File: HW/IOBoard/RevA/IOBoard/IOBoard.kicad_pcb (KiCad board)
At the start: 2 copper layers, 35.6 x 61 mm, 8 parts, among them J1 Conn_02x05_Odd_Even, J2 Conn_Coaxial, J3 Conn_Coaxial, J4 Conn_Coaxial

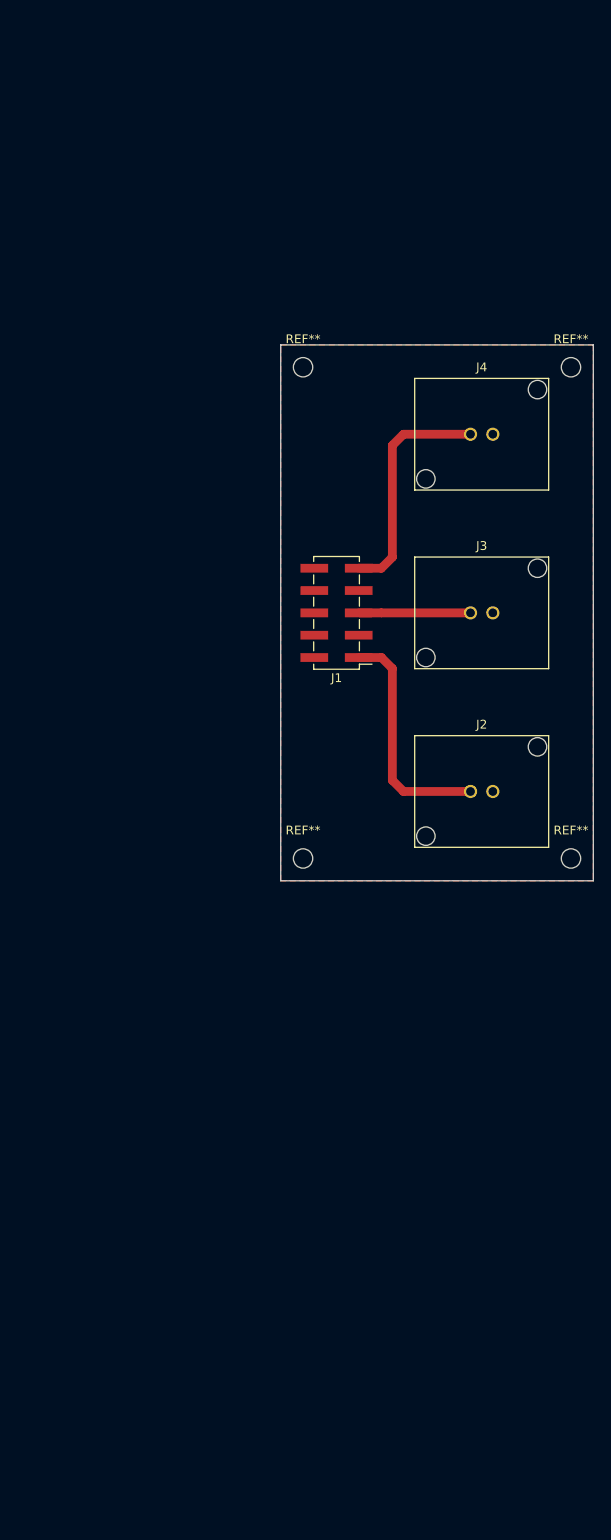
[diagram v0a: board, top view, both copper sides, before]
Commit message: updated front panel board layouts
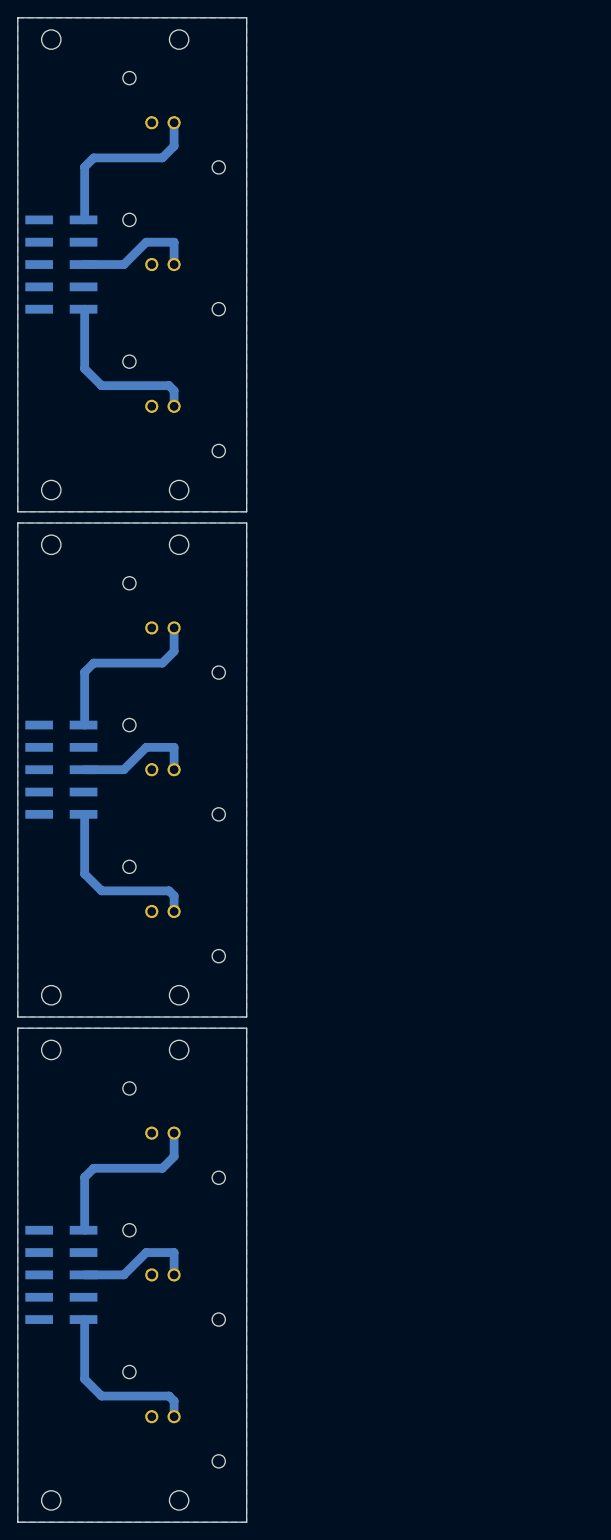
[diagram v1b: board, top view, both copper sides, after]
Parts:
- removed the J1 at (161.3, 85.1)
- removed the J2 at (177.8, 105.4)
- removed the J3 at (177.8, 85.1)
- removed the J4 at (177.8, 64.8)
- removed the REF** at (188.0, 113.0)
- removed the REF** at (157.5, 113.0)
- removed the REF** at (157.5, 57.1)
- removed the REF** at (188.0, 57.1)
- added J1: Conn_02x05_Odd_Even, Connector_PinHeader_2.54mm:PinHeader_2x05_P2.54mm_Vertical_SMD, B.Cu at (130.0, 160.4)
- added J1: Conn_02x05_Odd_Even, Connector_PinHeader_2.54mm:PinHeader_2x05_P2.54mm_Vertical_SMD, B.Cu at (130.0, 102.9)
- added J1: Conn_02x05_Odd_Even, Connector_PinHeader_2.54mm:PinHeader_2x05_P2.54mm_Vertical_SMD, B.Cu at (130.0, 45.5)
- added J2: Conn_Coaxial, RSProStraight50OhmPCBMountBulkheadFittingBNC_5260279:RSProStraight50OhmPCBMountBulkheadFittingBNC_5260279, B.Cu at (142.8, 144.3)
- added J2: Conn_Coaxial, RSProStraight50OhmPCBMountBulkheadFittingBNC_5260279:RSProStraight50OhmPCBMountBulkheadFittingBNC_5260279, B.Cu at (142.8, 86.8)
- added J2: Conn_Coaxial, RSProStraight50OhmPCBMountBulkheadFittingBNC_5260279:RSProStraight50OhmPCBMountBulkheadFittingBNC_5260279, B.Cu at (142.8, 29.3)
- added J3: Conn_Coaxial, RSProStraight50OhmPCBMountBulkheadFittingBNC_5260279:RSProStraight50OhmPCBMountBulkheadFittingBNC_5260279, B.Cu at (142.8, 160.4)
- added J3: Conn_Coaxial, RSProStraight50OhmPCBMountBulkheadFittingBNC_5260279:RSProStraight50OhmPCBMountBulkheadFittingBNC_5260279, B.Cu at (142.8, 102.9)
- added J3: Conn_Coaxial, RSProStraight50OhmPCBMountBulkheadFittingBNC_5260279:RSProStraight50OhmPCBMountBulkheadFittingBNC_5260279, B.Cu at (142.8, 45.5)
- added J4: Conn_Coaxial, RSProStraight50OhmPCBMountBulkheadFittingBNC_5260279:RSProStraight50OhmPCBMountBulkheadFittingBNC_5260279, B.Cu at (142.8, 176.5)
- added J4: Conn_Coaxial, RSProStraight50OhmPCBMountBulkheadFittingBNC_5260279:RSProStraight50OhmPCBMountBulkheadFittingBNC_5260279, B.Cu at (142.8, 119.1)
- added J4: Conn_Coaxial, RSProStraight50OhmPCBMountBulkheadFittingBNC_5260279:RSProStraight50OhmPCBMountBulkheadFittingBNC_5260279, B.Cu at (142.8, 61.6)
- added REF**: MountingHole_2.2mm_M2, MountingHole:MountingHole_2.2mm_M2, F.Cu at (128.8, 186.1)
- added REF**: MountingHole_2.2mm_M2, MountingHole:MountingHole_2.2mm_M2, F.Cu at (128.8, 19.9)
- added REF**: MountingHole_2.2mm_M2, MountingHole:MountingHole_2.2mm_M2, F.Cu at (128.8, 71.1)
- added REF**: MountingHole_2.2mm_M2, MountingHole:MountingHole_2.2mm_M2, F.Cu at (143.4, 19.9)
- added REF**: MountingHole_2.2mm_M2, MountingHole:MountingHole_2.2mm_M2, F.Cu at (128.8, 134.8)
- added REF**: MountingHole_2.2mm_M2, MountingHole:MountingHole_2.2mm_M2, F.Cu at (143.4, 134.8)
- added REF**: MountingHole_2.2mm_M2, MountingHole:MountingHole_2.2mm_M2, F.Cu at (143.4, 186.1)
- added REF**: MountingHole_2.2mm_M2, MountingHole:MountingHole_2.2mm_M2, F.Cu at (128.8, 128.6)
- added REF**: MountingHole_2.2mm_M2, MountingHole:MountingHole_2.2mm_M2, F.Cu at (128.8, 77.3)
- added REF**: MountingHole_2.2mm_M2, MountingHole:MountingHole_2.2mm_M2, F.Cu at (143.4, 77.3)
- added REF**: MountingHole_2.2mm_M2, MountingHole:MountingHole_2.2mm_M2, F.Cu at (143.4, 128.6)
- added REF**: MountingHole_2.2mm_M2, MountingHole:MountingHole_2.2mm_M2, F.Cu at (143.4, 71.1)
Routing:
- net (no net): track 0.00 -> 106.5 mm
- net /TRIG_SIG_IN: track 26.5 -> 19.7 mm
- net /FUNC_SYNC_OUT: track 26.5 -> 19.8 mm
- net /FUNC_SIG_OUT: track 12.7 -> 13.8 mm
- added copper zone on B.Cu, net (none)
- added copper zone on B.Cu, net GNDS
- removed copper zone on F.Cu, net GNDS
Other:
- board size 35.6 x 61 mm -> 26 x 171.1 mm
- board text added: "Print Layers: - B.Cu - Dwgs.User Print options: - "Exclude PCB edge" = True - "MIrrored" = TRUE"

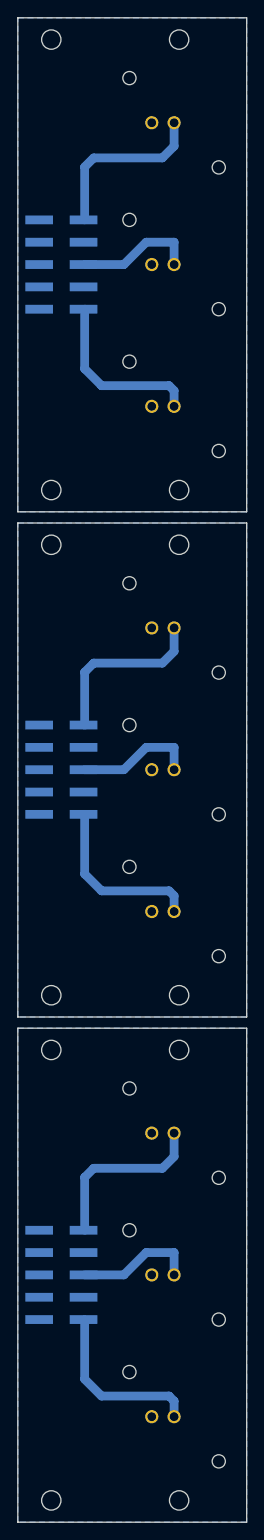
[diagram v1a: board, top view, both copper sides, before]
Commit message: Added Revb designs for I/O and control panels
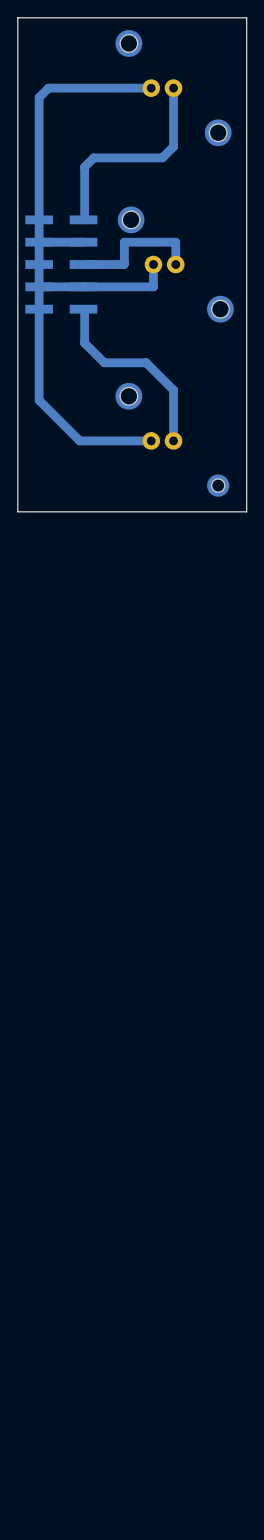
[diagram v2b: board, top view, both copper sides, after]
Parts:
- removed the J1 at (130.0, 160.4)
- removed the J1 at (130.0, 102.9)
- removed the J2 at (142.8, 144.3)
- removed the J2 at (142.8, 86.8)
- removed the J3 at (142.8, 160.4)
- removed the J3 at (142.8, 102.9)
- removed the J4 at (142.8, 176.5)
- removed the J4 at (142.8, 119.1)
- removed REF** (x12): MountingHole_2.2mm_M2, MountingHole:MountingHole_2.2mm_M2
- moved J2 3.94 mm to (142.7, 25.4)
- moved J4 3.94 mm to (142.7, 65.5)
- moved J3 0.19 mm to (143.0, 45.5)
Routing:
- net (no net): track 106.5 -> 0.00 mm
- net GNDS: track 0.00 -> 82.9 mm
- net /FUNC_SYNC_OUT: track 19.8 -> 23.5 mm
- net /TRIG_SIG_IN: track 19.7 -> 22.0 mm
- net /FUNC_SIG_OUT: track 13.8 -> 15.4 mm
- removed copper zone on B.Cu, net (none)
- removed copper zone on B.Cu, net GNDS
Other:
- board size 26 x 171.1 mm -> 26 x 56.2 mm
